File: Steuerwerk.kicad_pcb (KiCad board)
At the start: 2 copper layers, 100 x 160 mm, 124 parts, among them J1 2PinTerminalBlocktg, J10 2PinTerminalBlocktg, J11 2PinTerminalBlocktg, J12 2PinTerminalBlocktg, J2 2PinTerminalBlocktg, J3 3PinTerminalBlocktg, J4 3PinTerminalBlocktg, J5 2PinTerminalBlocktg, J6 2PinTerminalBlocktg, J7 2PinTerminalBlocktg, J8 2PinTerminalBlocktg, J9 2PinTerminalBlocktg, Q1 Q_PNP_BCE, U1 74ls240, U2 74541, U3 74LS161, U4 74LS138, U5 74LS138, U6 74541, U7 74LS374, U8 74LS374

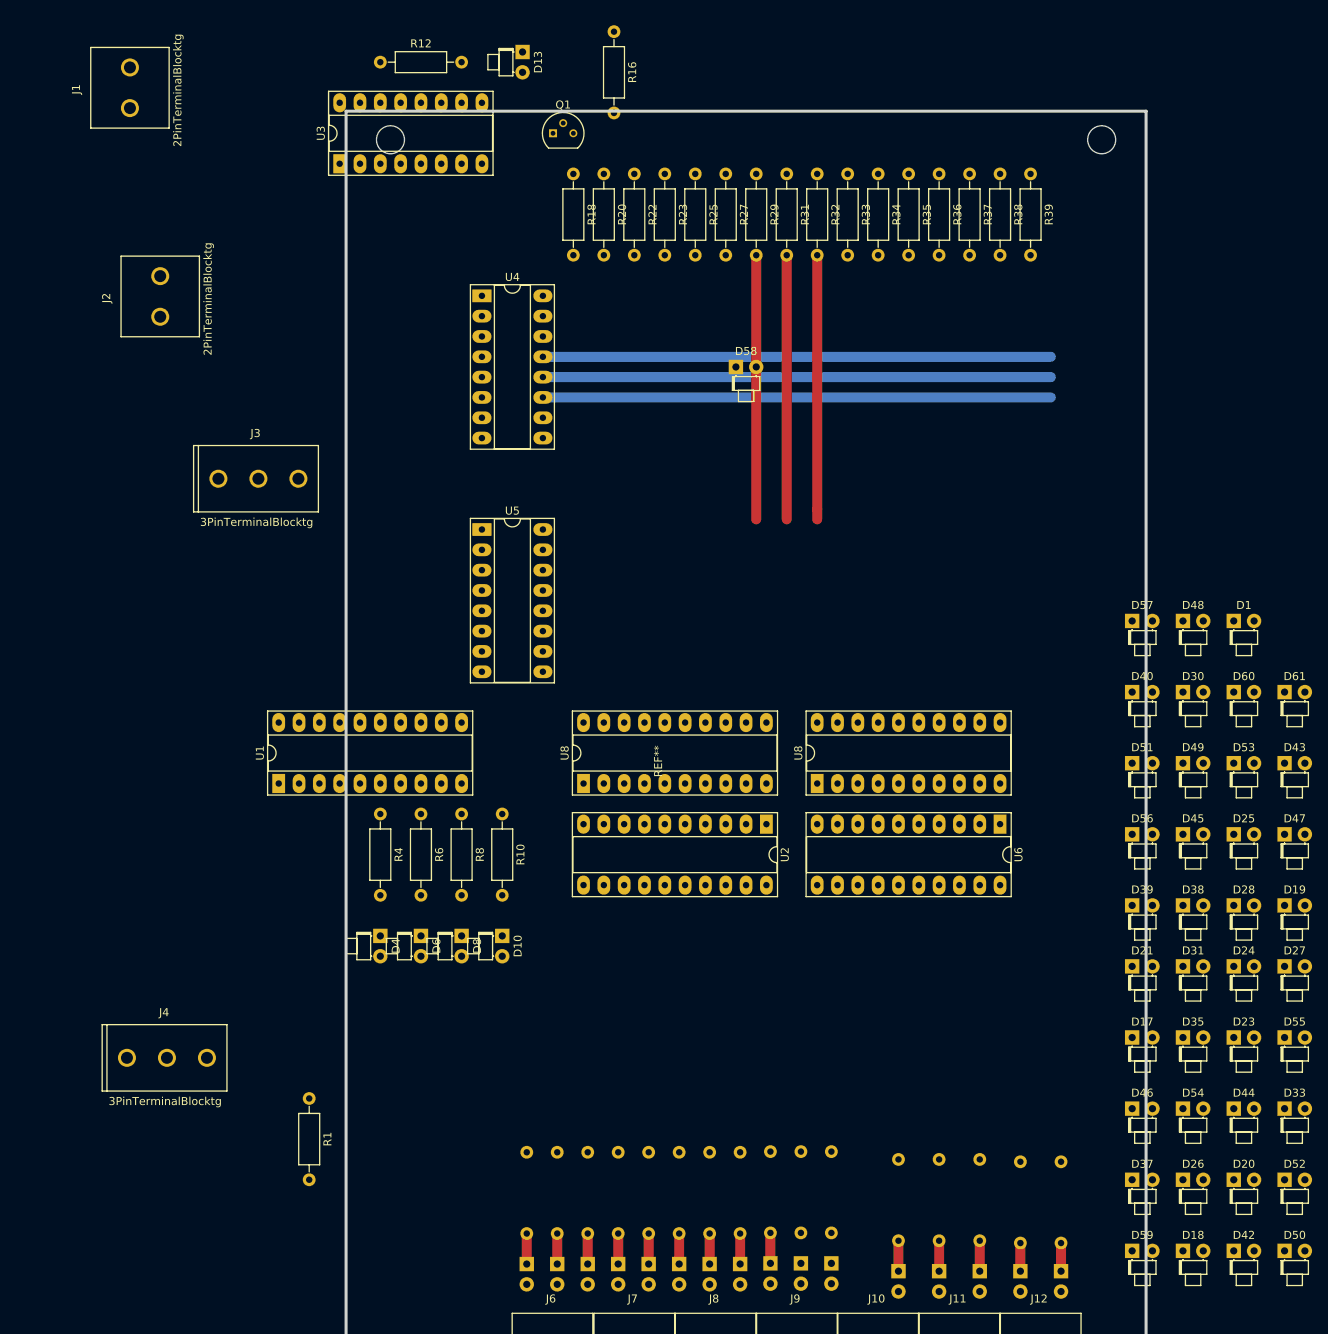
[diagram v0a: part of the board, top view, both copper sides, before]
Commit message: todo smaler LED done
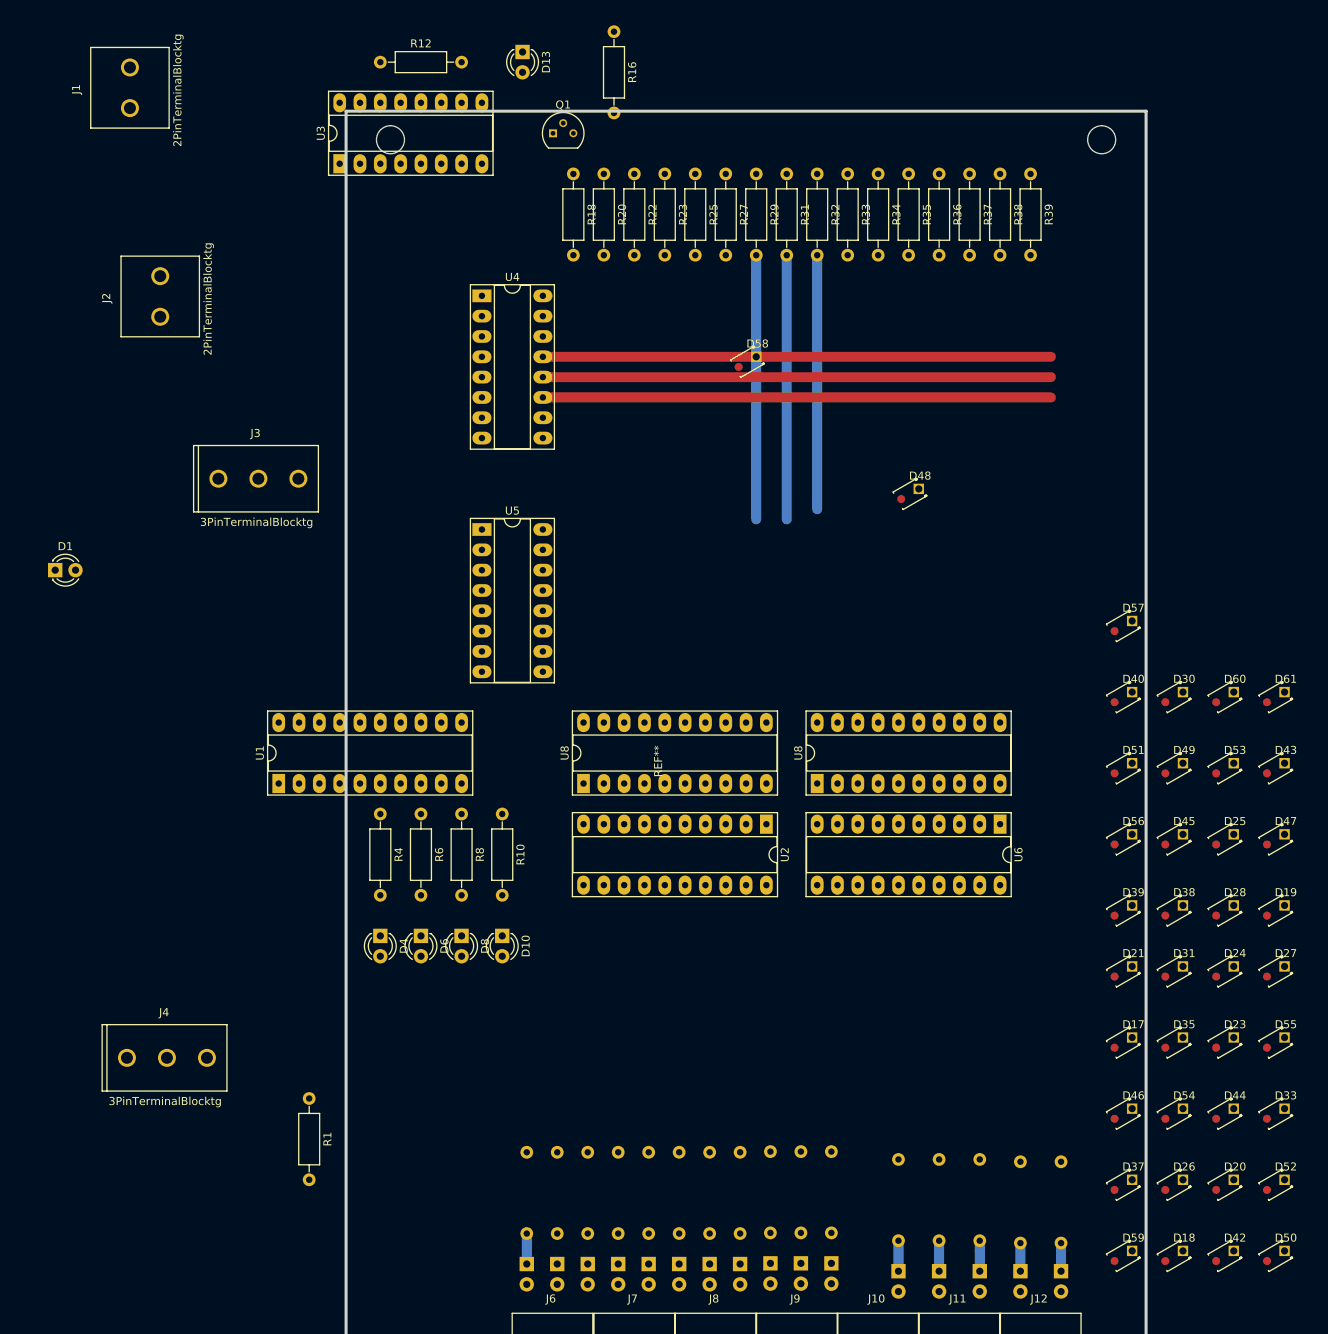
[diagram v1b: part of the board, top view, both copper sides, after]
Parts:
- D1, D10, D13, D4, D6, D8: footprint LEDs:LED_D1.8mm_W1.8mm_H2.4mm_Horizontal_O1.27mm_Z4.9mm -> LEDs:LED_D3.0mm
- D11, D12, D14, D15, D16, D2, D22, D29, D3, D32, D34, D36, D41, D5, D7, D9: footprint LEDs:LED_D1.8mm_W1.8mm_H2.4mm_Horizontal_O1.27mm_Z4.9mm -> LEDs:LED_D1.8mm_W1.8mm_H2.4mm_Horizontal_O1.27mm_Z1.6mm
- D17, D18, D19, D20, D21, D23, D24, D25, D26, D27, D28, D30, D31, D33, D35, D37, D38, D39, D40, D42, D43, D44, D45, D46, D47, D48, D49, D50, D51, D52, D53, D54, D55, D56, D57, D58, D59, D60, D61: footprint LEDs:LED_D1.8mm_W1.8mm_H2.4mm_Horizontal_O1.27mm_Z4.9mm -> tg_foodprint:LED_D1.8mm_W3.3mm_H2.4mmBonsai
- moved D1 147.5 mm to (5.08, 101.6)
- moved D48 36.9 mm to (113.0, 91.4)
- moved D58 2.84 mm to (92.7, 74.9)
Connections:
- D46 pad 2: Net-(D43-Pad1) -> Net-(D46-Pad2)
- R34 pad 2: Net-(D43-Pad1) -> Net-(D46-Pad2)
- U8 pad 8: Net-(D43-Pad1) -> Net-(D46-Pad2)
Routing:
- net Net-(D9-Pad1): track 3.81 -> 0.00 mm
- net Net-(D7-Pad1): track 3.81 -> 0.00 mm
- net Net-(D5-Pad1): track 3.81 -> 0.00 mm
- net Net-(D3-Pad1): track 3.81 -> 0.00 mm
- net Net-(D15-Pad1): track 3.81 -> 0.00 mm
- net Net-(D14-Pad1): track 3.81 -> 0.00 mm
- net Net-(D12-Pad1): track 3.81 -> 0.00 mm
- net Net-(D11-Pad1): track 3.81 -> 0.00 mm
- net /Takt: track 33.0 -> 31.8 mm

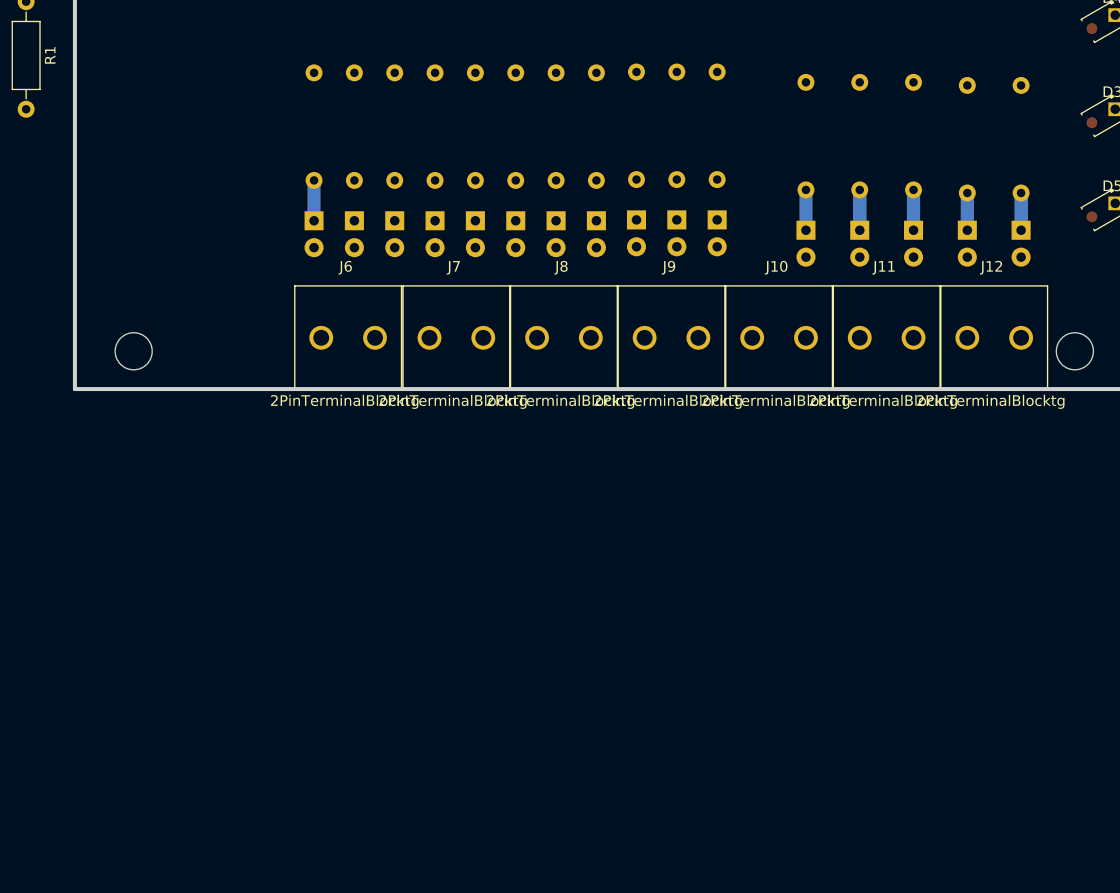
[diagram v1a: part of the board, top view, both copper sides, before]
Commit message: changed cupper front layer to bottom layer
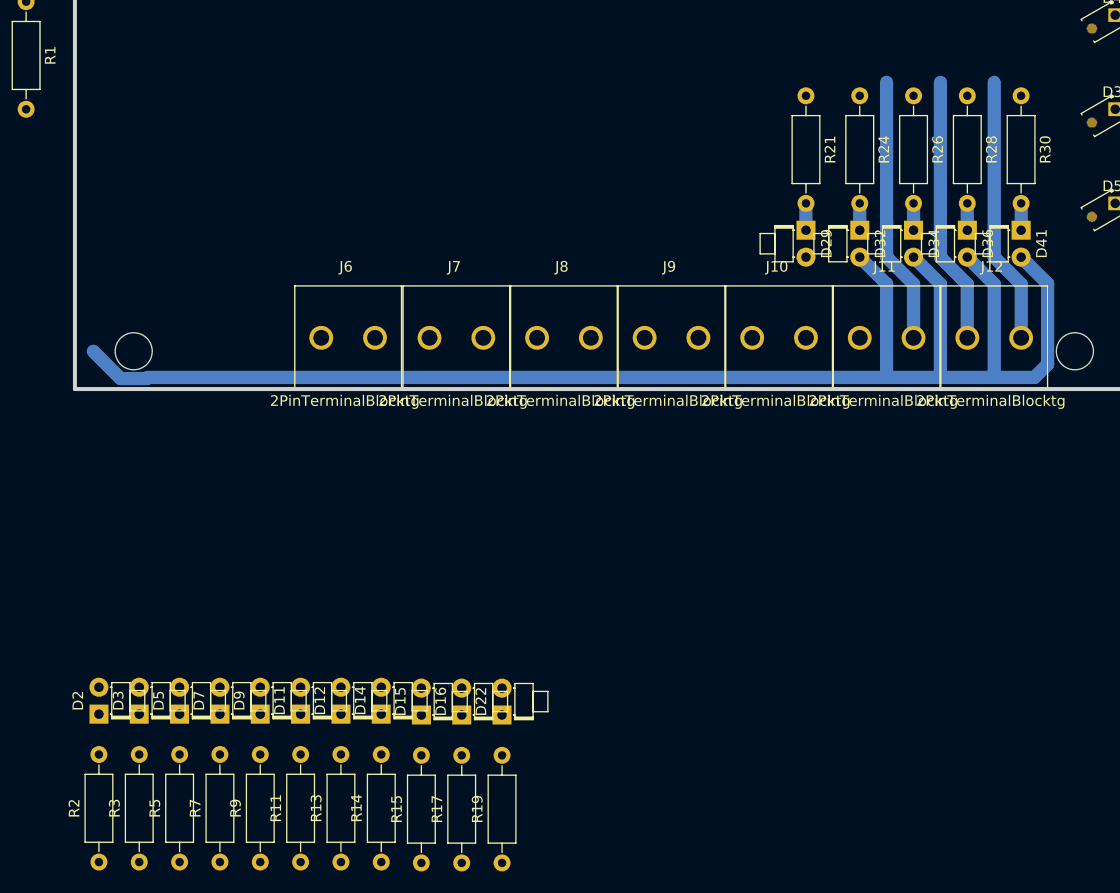
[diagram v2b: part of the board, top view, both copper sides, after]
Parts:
- D11, D12, D14, D15, D16, D2, D22, D29, D3, D32, D34, D36, D41, D5, D7, D9, R11, R13, R14, R15, R17, R19, R2, R21, R24, R26, R28, R3, R30, R5, R7, R9: moved to F.Cu
- moved R15 77.4 mm to (74.2, 249.0), turned to 90 degrees
- moved R17 77.4 mm to (78.0, 249.0), turned to 90 degrees
- moved R19 77.4 mm to (81.8, 249.0), turned to 90 degrees
- moved R11 77.3 mm to (62.8, 248.9), turned to 90 degrees
- moved R13 77.3 mm to (66.6, 248.9), turned to 90 degrees
- moved R14 77.3 mm to (70.4, 248.9), turned to 90 degrees
- moved R2 77.3 mm to (43.7, 248.9), turned to 90 degrees
- moved R3 77.3 mm to (47.5, 248.9), turned to 90 degrees
- moved R5 77.3 mm to (51.3, 248.9), turned to 90 degrees
- moved R7 77.3 mm to (55.1, 248.9), turned to 90 degrees
- moved R9 77.3 mm to (58.9, 248.9), turned to 90 degrees
- moved D15 51.0 mm to (74.2, 235.0), turned to 90 degrees
- moved D16 51.0 mm to (78.0, 235.0), turned to 90 degrees
- moved D22 51.0 mm to (81.8, 235.0), turned to 90 degrees
- moved D11 50.8 mm to (62.8, 234.9), turned to 90 degrees
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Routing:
- net VCC: track 0.00 -> 140.2 mm
- net /16: track 0.00 -> 25.2 mm
- net /13: track 0.00 -> 25.2 mm
- net /15: track 0.00 -> 25.2 mm
- net Net-(D2-Pad1): track 3.81 -> 0.00 mm
- net Net-(D34-Pad1): track 3.81 -> 2.54 mm
- net Net-(D32-Pad1): track 3.81 -> 2.54 mm
- net Net-(D29-Pad1): track 3.81 -> 2.54 mm
- net Net-(D41-Pad1): track 3.52 -> 2.54 mm
- net Net-(D36-Pad1): track 3.52 -> 2.54 mm

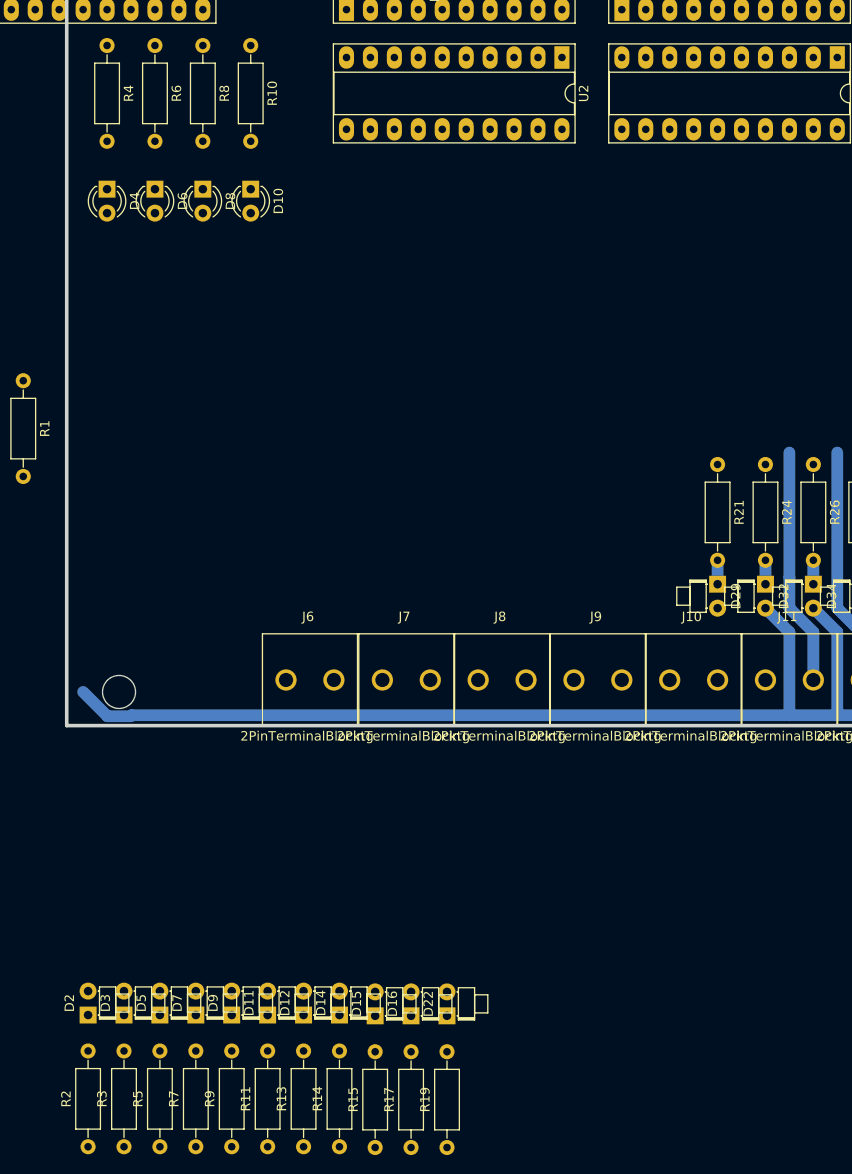
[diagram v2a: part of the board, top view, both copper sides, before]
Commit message: weitere Leiterbahnen hinzugefügt
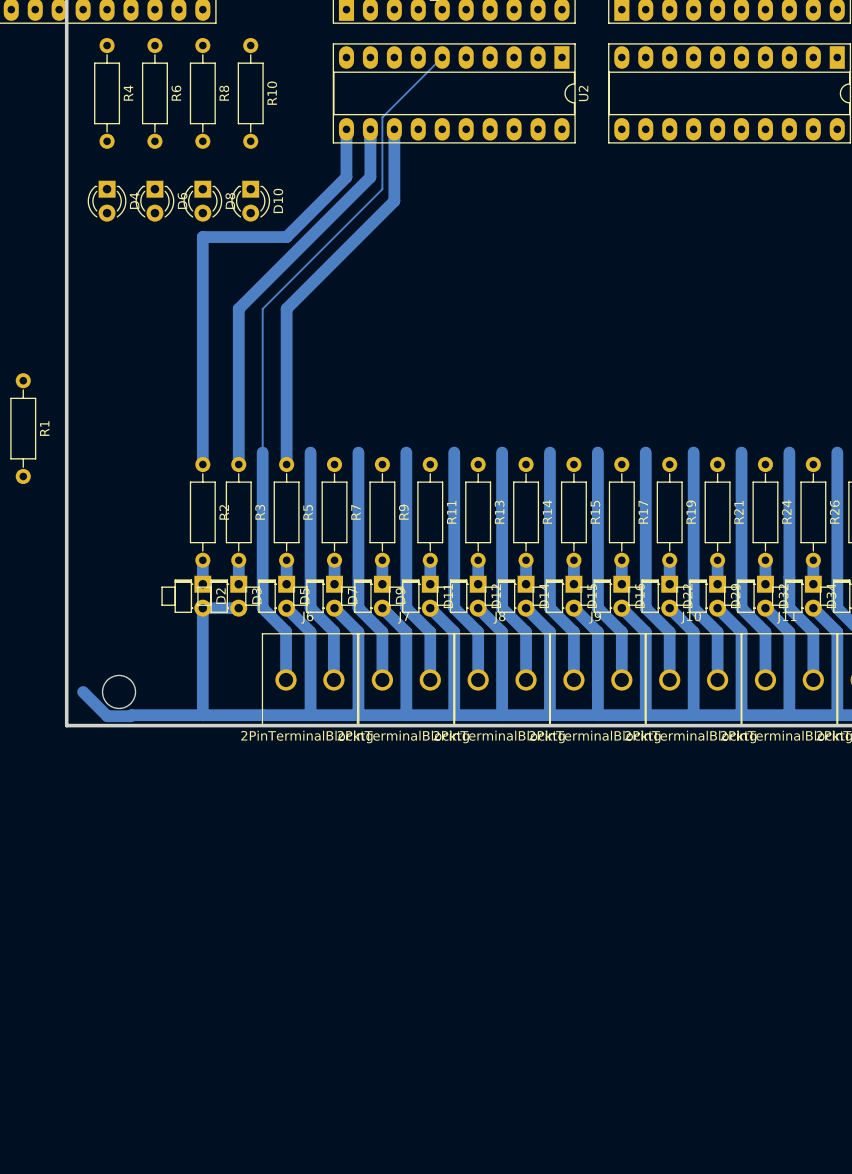
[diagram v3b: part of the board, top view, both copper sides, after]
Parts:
- moved R19 76.2 mm to (105.4, 176.5), turned to 270 degrees
- moved R17 75.8 mm to (100.3, 176.5), turned to 270 degrees
- moved R15 75.5 mm to (95.2, 176.5), turned to 270 degrees
- moved R14 75.0 mm to (90.2, 176.5), turned to 270 degrees
- moved R13 74.7 mm to (85.1, 176.5), turned to 270 degrees
- moved R11 74.4 mm to (80.0, 176.5), turned to 270 degrees
- moved R9 74.1 mm to (74.9, 176.5), turned to 270 degrees
- moved R7 73.9 mm to (69.8, 176.5), turned to 270 degrees
- moved R5 73.6 mm to (64.8, 176.5), turned to 270 degrees
- moved R2 73.4 mm to (55.9, 176.5), turned to 270 degrees
- moved R3 73.4 mm to (59.7, 176.5), turned to 270 degrees
- moved D22 51.5 mm to (105.4, 189.2), turned to 270 degrees
- moved D16 51.0 mm to (100.3, 189.2), turned to 270 degrees
- moved D15 50.4 mm to (95.2, 189.2), turned to 270 degrees
- moved D14 49.8 mm to (90.2, 189.2), turned to 270 degrees
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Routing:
- net VCC: track 140.2 -> 279.4 mm
- net Net-(J6-Pad1): track 0.00 -> 75.0 mm
- net Net-(R2-Pad1): track 0.00 -> 47.1 mm
- net Net-(R3-Pad1): track 0.00 -> 42.6 mm
- net Net-(R5-Pad1): track 0.00 -> 40.3 mm
- net Net-(J9-Pad1): track 0.00 -> 25.2 mm
- net Net-(J7-Pad1): track 0.00 -> 25.2 mm
- net /enAkku: track 0.00 -> 25.2 mm
- net /7: track 0.00 -> 25.2 mm
- net /5: track 0.00 -> 25.2 mm
- net Net-(J11-Pad1): track 0.00 -> 25.2 mm
- net Net-(J10-Pad1): track 0.00 -> 25.2 mm
- net /9: track 0.00 -> 25.2 mm
- net /11: track 0.00 -> 25.2 mm
- net /3: track 0.00 -> 25.2 mm
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
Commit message: Verbindungen zum IC fortgeführt
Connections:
- J6 pad 1: Net-(J6-Pad1) -> /3
- J6 pad 2: /3 -> Net-(J6-Pad2)
- J7 pad 1: Net-(J7-Pad1) -> /5
- J7 pad 2: /5 -> Net-(J7-Pad2)
- J8 pad 1: /enAkku -> /7
- J8 pad 2: /7 -> /enAkku
- U2 pad 4: Net-(J7-Pad1) -> Net-(J7-Pad2)
- U2 pad 6: Net-(J6-Pad1) -> Net-(J6-Pad2)
- U7 pad 15: Net-(J7-Pad1) -> Net-(J7-Pad2)
- U7 pad 9: Net-(J6-Pad1) -> Net-(J6-Pad2)
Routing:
- net Net-(J6-Pad1): track 75.0 -> 0.00 mm
- net Net-(J6-Pad2): track 0.00 -> 72.9 mm
- net Net-(J7-Pad2): track 0.00 -> 70.8 mm
- net /3: track 25.2 -> 73.9 mm
- net /5: track 25.2 -> 71.8 mm
- net /7: track 25.2 -> 69.7 mm
- net /enAkku: track 25.2 -> 68.7 mm
- net Net-(R7-Pad1): track 0.00 -> 39.2 mm
- net Net-(R9-Pad1): track 0.00 -> 38.2 mm
- net Net-(R11-Pad1): track 0.00 -> 37.1 mm
- net Net-(R14-Pad1): track 0.00 -> 36.1 mm
- net Net-(R13-Pad1): track 0.00 -> 36.1 mm
- net Net-(J7-Pad1): track 25.2 -> 0.00 mm
